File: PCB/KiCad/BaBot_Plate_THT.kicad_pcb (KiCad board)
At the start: 2 copper layers, 100 x 101.5 mm, 62 parts, among them Q1 1540031NC6090, Q10 1540031NC6090, Q11 1540031NC6090, Q12 1540031NC6090, Q13 1540031NC6090, Q14 1540031NC6090, Q15 1540031NC6090, Q16 1540031NC6090, Q17 FQP30N06L, Q2 1540031NC6090, Q3 1540031NC6090, Q4 1540031NC6090, Q5 1540031NC6090, Q6 1540031NC6090, Q7 1540031NC6090, Q8 1540031NC6090, Q9 1540031NC6090, U1 20-way header to Base

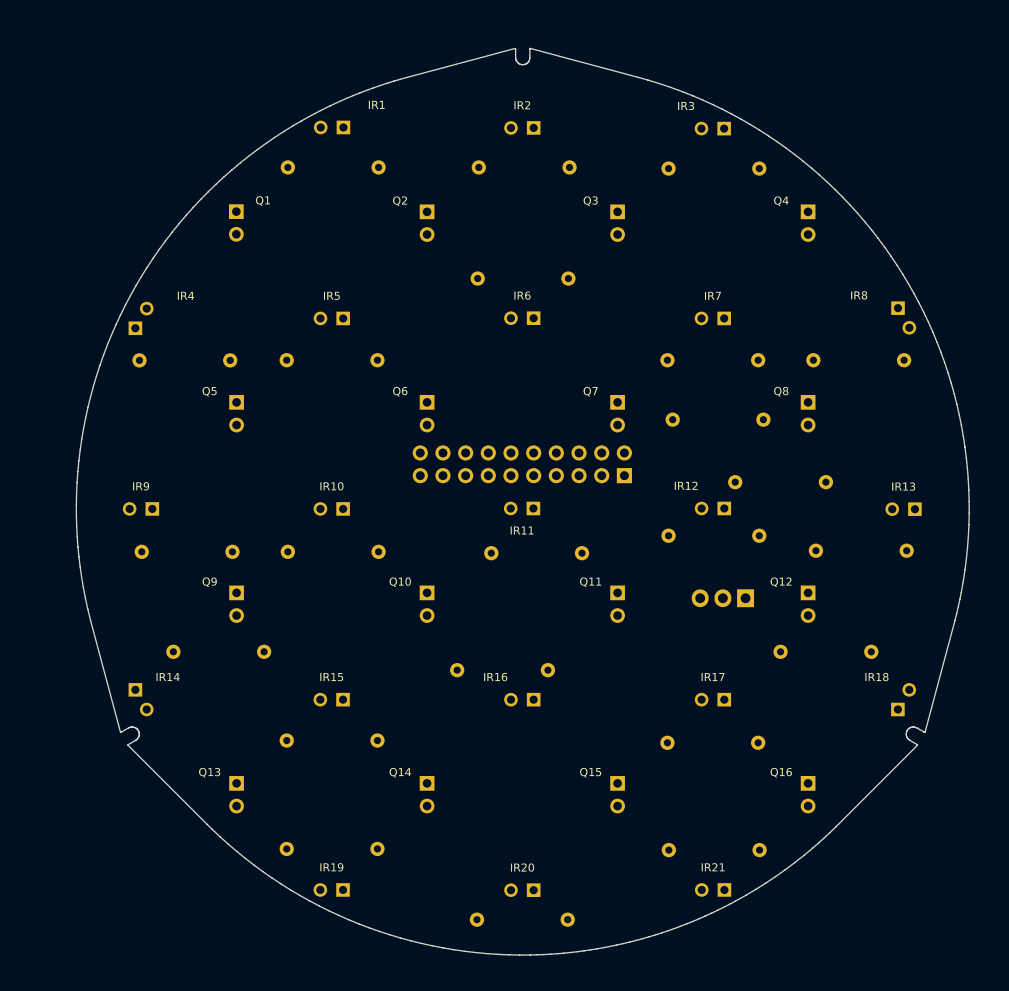
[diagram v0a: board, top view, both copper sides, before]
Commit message: Integrate routed two-layer THT Plate PCB and fabrication package
Plate layout by liu andy (https://github.com/andy100056en12-sys).
Integrate the routed KiCad board, Gerber/drill ZIP, mask-corrected footprints,
and fabrication notes. Archive the unrouted Plate and rejected maskless export.

Validation: Plate PCB DRC 0 violations and 0 unconnected items; both mask
plots have 143 openings and the plated drill plot has 162 hits.
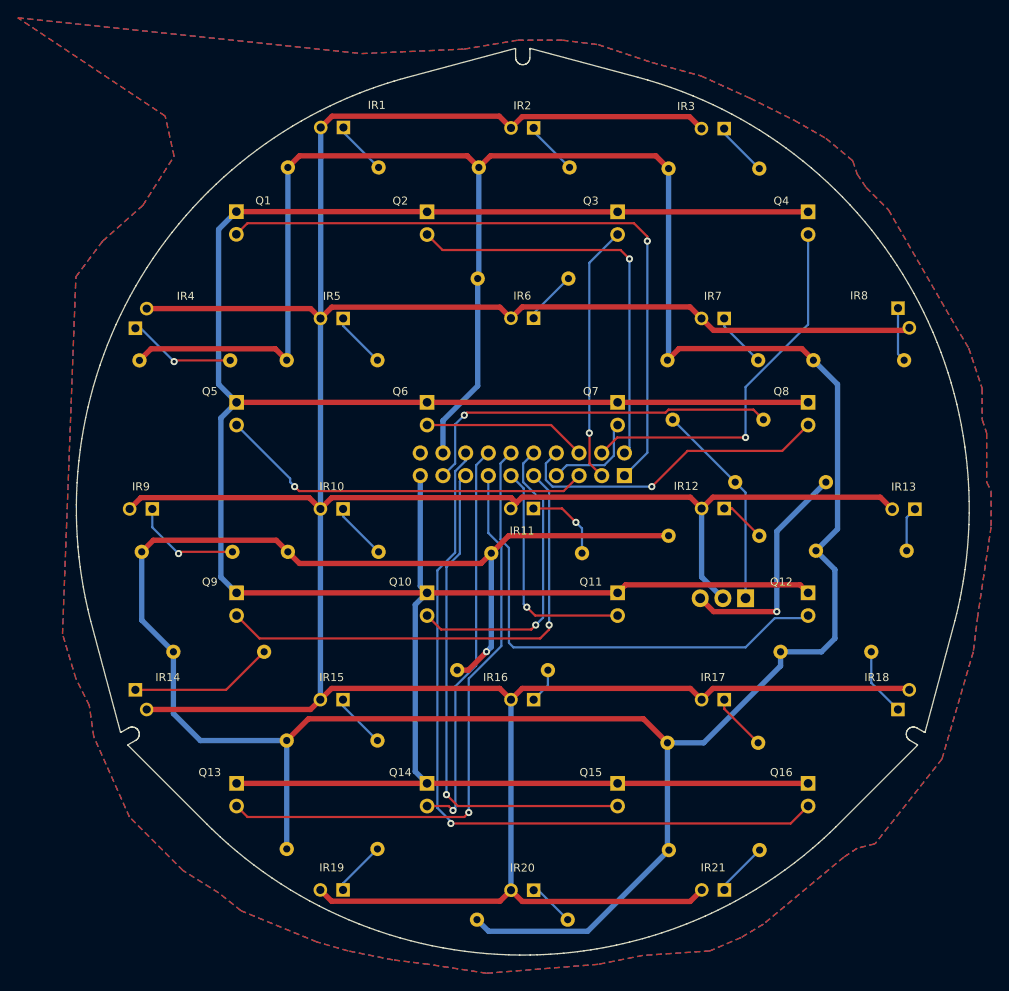
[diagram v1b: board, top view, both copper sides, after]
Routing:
- net IR_CATHODES: track 0.00 -> 453.2 mm
- net +5V_SERVO: track 0.00 -> 420.9 mm, vias 0 -> 1
- net +5V_LOGIC: track 0.00 -> 338.8 mm
- net PT15: track 0.00 -> 84.2 mm, vias 0 -> 1
- net PT00: track 0.00 -> 75.0 mm, vias 0 -> 1
- net PT12: track 0.00 -> 66.6 mm, vias 0 -> 1
- net PT11: track 0.00 -> 57.3 mm
- net PT14: track 0.00 -> 56.3 mm, vias 0 -> 1
- net PT08: track 0.00 -> 54.4 mm, vias 0 -> 1
- net PT01: track 0.00 -> 45.8 mm, vias 0 -> 1
- net PT13: track 0.00 -> 44.8 mm, vias 0 -> 1
- net PT03: track 0.00 -> 42.5 mm, vias 0 -> 1
- net PT04: track 0.00 -> 42.4 mm, vias 0 -> 1
- net IR_LED_CONTROL: track 0.00 -> 42.0 mm, vias 0 -> 1
- net PT07: track 0.00 -> 36.0 mm, vias 0 -> 1
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- added copper zone on B.Cu, net GND
- added copper zone on F.Cu, net GND
